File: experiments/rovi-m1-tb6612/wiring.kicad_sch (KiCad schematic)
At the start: 4 parts, among them M1 DC_MOTOR, U1 ESP32S3, U2 TB6612FNG

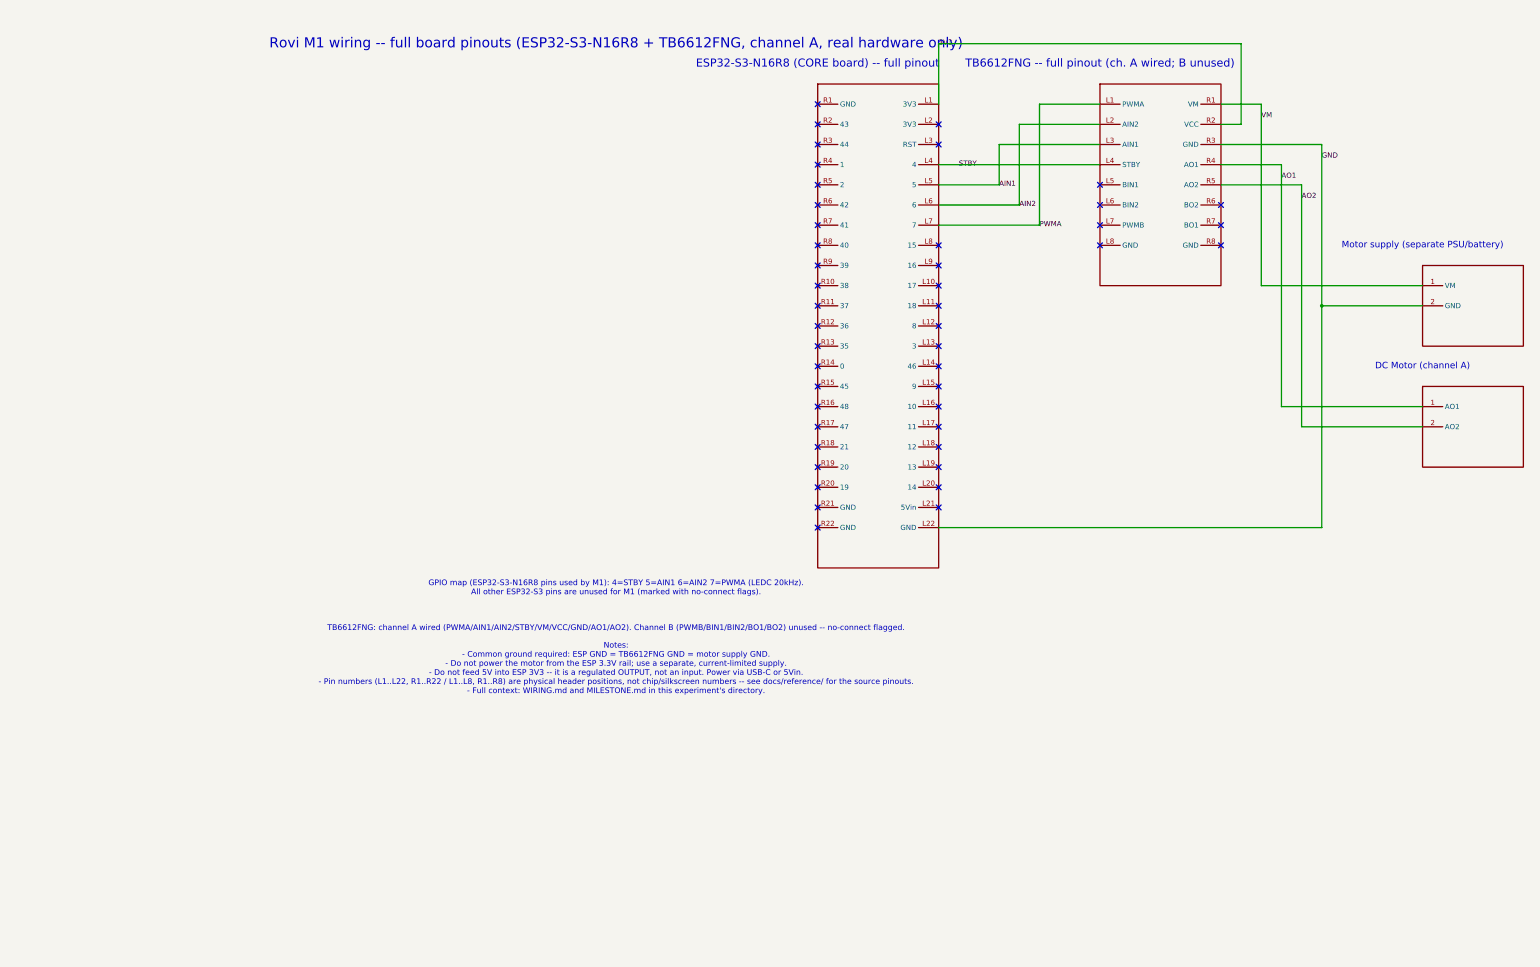
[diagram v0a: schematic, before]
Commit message: M1: switch to native MCPWM, fix TB6612FNG pinout orientation
- Switch PWMA generation from LEDC to the ESP32-S3's native MCPWM
  peripheral (esp-hal mcpwm), which is a drop-in for tb6612fng's
  SetDutyCycle-based Motor since both implement embedded-hal::pwm.
- Correct the TB6612FNG left/right header assignment: the reference
  photo was of the board's bottom, not top, so docs/reference and
  wiring.kicad_sch had it mirrored.
- Rebuild wiring.kicad_sch from a generator script with a corrected
  layout (driver left of controller, motor/PSU further left) so L/R
  pins exit their true physical side and facing headers wire directly
  across with minimal crossings; also fixes overlapping Motor/PSU
  symbol boxes.
- Flag GPIO35-37 as PSRAM-reserved on the N16R8 (octal PSRAM) module.
- Add docs/reference/kicad-authoring.md and
  scripts/check-kicad-labels.py, capturing the pin-geometry formulas
  and the label-on-wire net-merge trap hit while rebuilding the
  schematic.
- Add Taskfile m1:build/m1:flash targets; fix shell.nix's
  pkgs.taskfile -> pkgs.go-task (the wrong attribute name broke the
  whole dev shell, not just task).

Co-Authored-By: Claude Sonnet 5 <noreply@anthropic.com>
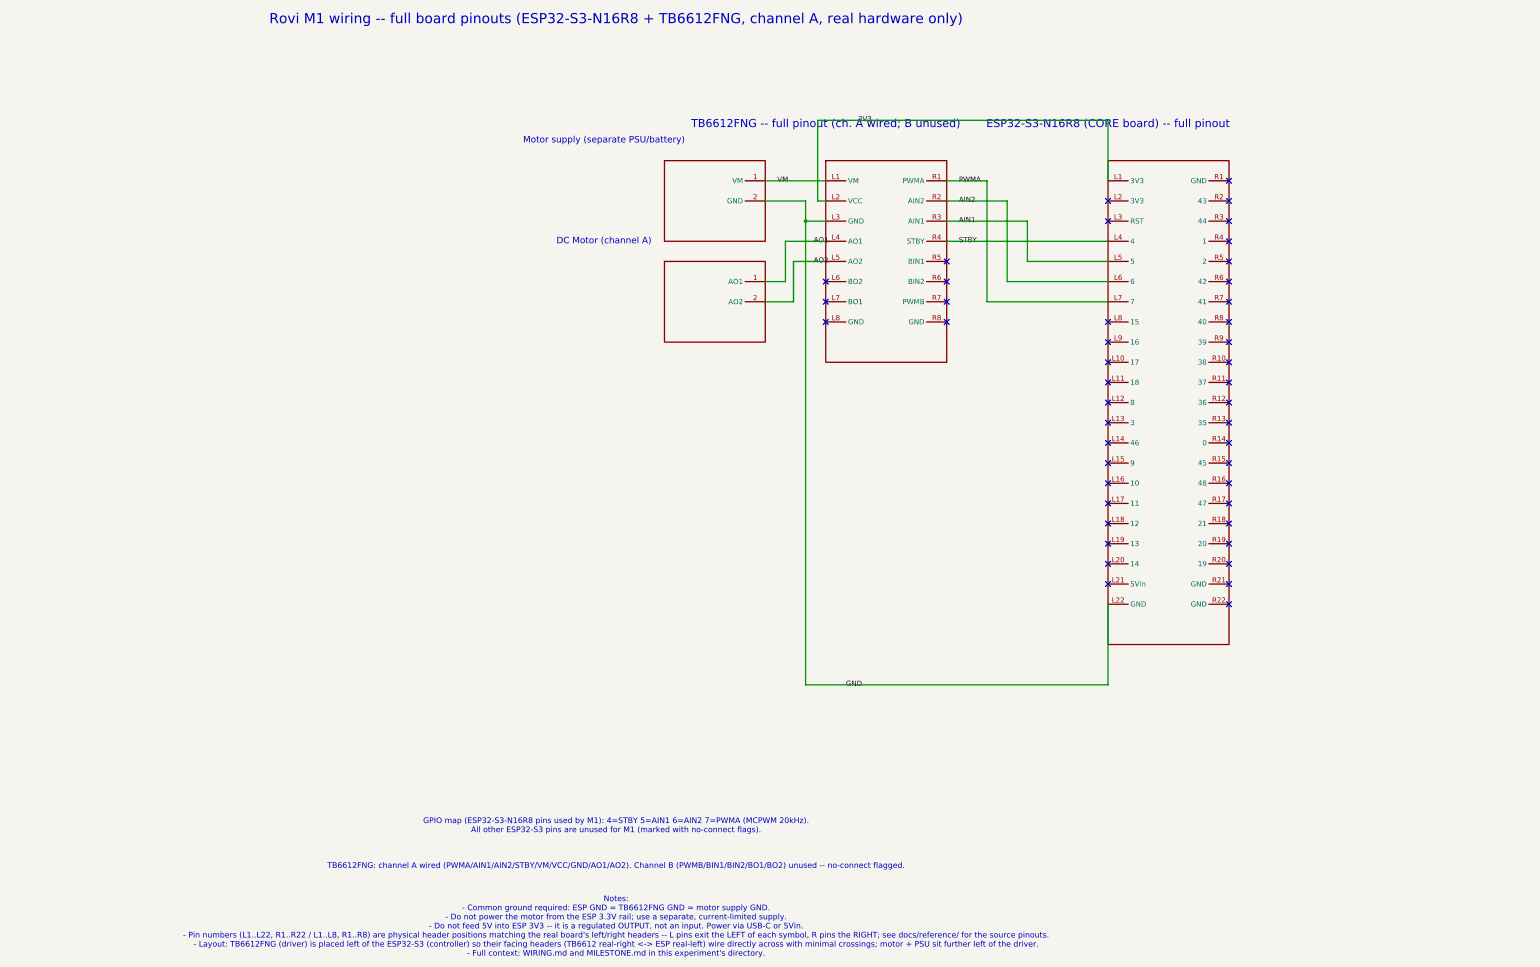
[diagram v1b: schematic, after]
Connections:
- net 3V3: now also U2.L2 (VCC); no longer U2.R2 (VCC)
- net AIN1: now also U2.R3 (AIN1); no longer U2.L3 (AIN1)
- net AIN2: now also U2.R2 (AIN2); no longer U2.L2 (AIN2)
- net AO1: now also U2.L4 (AO1); no longer U2.R4 (AO1)
- net AO2: now also U2.L5 (AO2); no longer U2.R5 (AO2)
- net GND: now also U2.L3 (GND); no longer U2.R3 (GND)
- net PWMA: now also U2.R1 (PWMA); no longer U2.L1 (PWMA)
- net STBY: now also U2.R4 (STBY); no longer U2.L4 (STBY)
- net VM: now also U2.L1 (VM); no longer U2.R1 (VM)
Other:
- note added: "GPIO map (ESP32-S3-N16R8 pins used by M1): 4=STBY 5=AIN1 6=AIN2 7=PWMA (MCPWM 20kHz). All other ESP32-S3 pins are unused for M1 (marked with no-connect flags)."
- note added: "Notes: - Common ground required: ESP GND = TB6612FNG GND = motor supply GND. - Do not power the motor from the ESP 3.3V rail; use a separate, current-limited supply. - Do not feed 5V into ESP 3V3 -- it is a regulated OUTPUT, not an input. Power via USB-C or 5Vin. - Pin numbers (L1..L22, R1..R22 / L1..L8, R1..R8) are physical header positions matching the real board's left/right headers -- L pins 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"
- note removed: "GPIO map (ESP32-S3-N16R8 pins used by M1): 4=STBY 5=AIN1 6=AIN2 7=PWMA (LEDC 20kHz). All other ESP32-S3 pins are unused for M1 (marked with no-connect flags)."
- note removed: "Notes: - Common ground required: ESP GND = TB6612FNG GND = motor supply GND. - Do not power the motor from the ESP 3.3V rail; use a separate, current-limited supply. - Do not feed 5V into ESP 3V3 -- it is a regulated OUTPUT, not an input. Power via USB-C or 5Vin. - Pin numbers (L1..L22, R1..R22 / L1..L8, R1..R8) are physical header positions, not chip/silkscreen numbers -- see docs/reference/ for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"
